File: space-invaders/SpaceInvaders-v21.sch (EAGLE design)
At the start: 26 parts, among them J2-J4 TM4C123GXL, J3-J1 TM4C123GXL, J5 NOKIA_5110, J6 NOKIA_5110, J7 9V, U1 LM7805CT

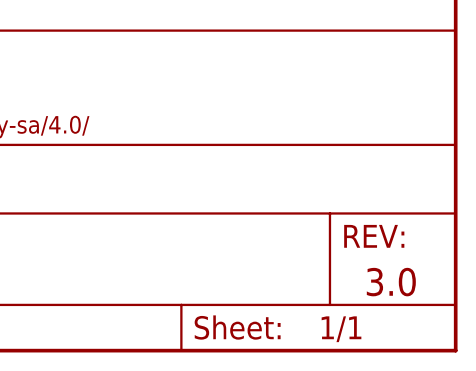
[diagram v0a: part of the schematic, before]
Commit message: Change the final version to 2.1
v3.0 and v2.1 are the same in structure. The only difference is that one
is supposed to made professionally by a fabrication house and the other
one is made by OtherMill.
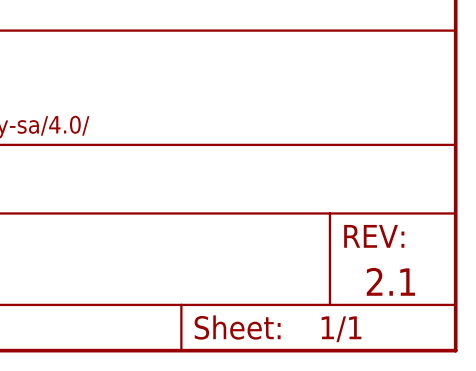
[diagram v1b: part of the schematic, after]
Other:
- note added: "2.1"
- note removed: "3.0"
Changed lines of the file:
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@@
 <plain>
 <text x="172.72" y="12.7" size="3.048" layer="94" font="vector" align="center-left">Phi Luu</text>
-<text x="238.76" y="7.62" size="3.048" layer="94" font="vector" align="center-left">3.0</text>
+<text x="238.76" y="7.62" size="3.048" layer="94" font="vector" align="center-left">2.1</text>
 <text x="134.62" y="147.32" size="1.778" layer="96" font="vector" rot="R90">PB0</text>
 <text x="132.08" y="147.32" size="1.778" layer="96" font="vector" rot="R90">PB1</text>

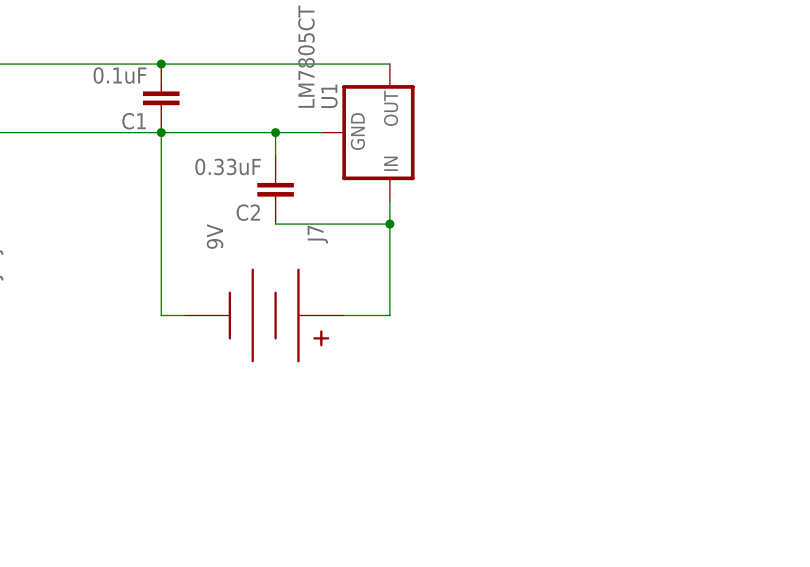
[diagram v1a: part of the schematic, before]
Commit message: Add SPDT power switch
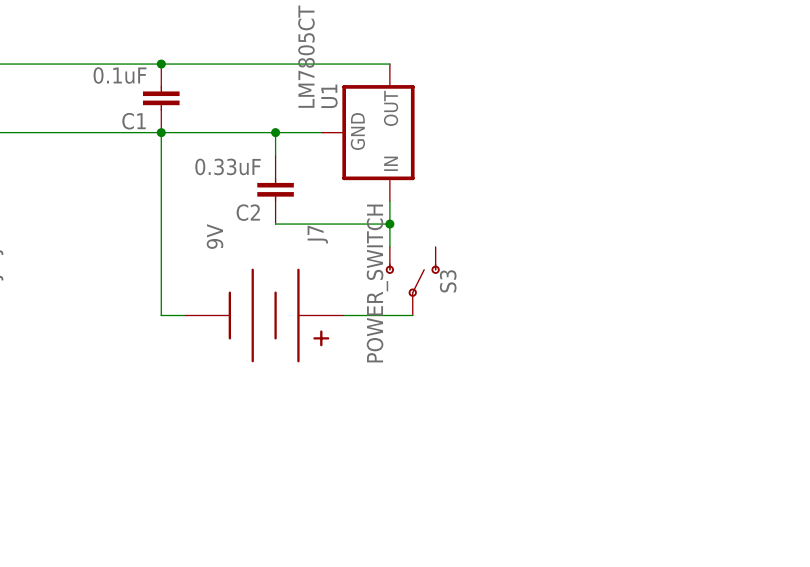
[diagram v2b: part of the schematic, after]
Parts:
- added S3: POWER_SWITCH, SparkFun-Switches:SWITCH-SPDT-PTH-11.6X4.0MM
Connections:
- new net VIN: J7.V+, S3.P
- net 9V: now also S3.S; no longer J7.V+
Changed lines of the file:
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@@
 <?xml version="1.0" encoding="utf-8"?>
 <!DOCTYPE eagle SYSTEM "eagle.dtd">
-<eagle version="8.0.1">
+<eagle version="8.0.2">
 <drawing>
 <settings>
@@
 <part name="S1" library="SparkFun-Switches" deviceset="MOMENTARY-SWITCH-SPST" device="-PTH-6.0MM" value="SPECIAL"/>
 <part name="S2" library="SparkFun-Switches" deviceset="MOMENTARY-SWITCH-SPST" device="-PTH-6.0MM" value="REGULAR"/>
+<part name="S3" library="SparkFun-Switches" deviceset="SWITCH-SPDT" device="-PTH-11.6X4.0MM" value="POWER_SWITCH"/>
 </parts>
 <sheets>
@@
 <instance part="S1" gate="G$1" x="101.6" y="50.8"/>
 <instance part="S2" gate="G$1" x="121.92" y="50.8"/>
+<instance part="S3" gate="1" x="190.5" y="101.6" rot="MR90"/>
 </instances>
 <busses>
@@
 <wire x1="187.96" y1="109.22" x2="187.96" y2="111.76" width="0.1524" layer="91"/>
 <wire x1="175.26" y1="109.22" x2="187.96" y2="109.22" width="0.1524" layer="91"/>
-<wire x1="187.96" y1="99.06" x2="187.96" y2="109.22" width="0.1524" layer="91"/>
+<pinref part="S3" gate="1" pin="S"/>
+<wire x1="187.96" y1="106.68" x2="187.96" y2="109.22" width="0.1524" layer="91"/>
 <junction x="187.96" y="109.22"/>
-<pinref part="J7" gate="G$1" pin="V+"/>
-<wire x1="182.88" y1="99.06" x2="187.96" y2="99.06" width="0.1524" layer="91"/>
 </segment>
 </net>
@@
 </segment>
 </net>
+<net name="VIN" class="1">
+<segment>
+<pinref part="J7" gate="G$1" pin="V+"/>
+<wire x1="182.88" y1="99.06" x2="190.5" y2="99.06" width="0.1524" layer="91"/>
+<pinref part="S3" gate="1" pin="P"/>
+</segment>
+</net>
